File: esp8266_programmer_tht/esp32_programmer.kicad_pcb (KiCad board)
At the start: 2 copper layers, 67.2 x 66.5 mm, 41 parts, among them P1 USB_C_Plug_USB2.0, Q1 S8050, Q2 S8050, SW1 SW_Push, SW2 SW_Push, U1 CH340C, U2 ESP-12E

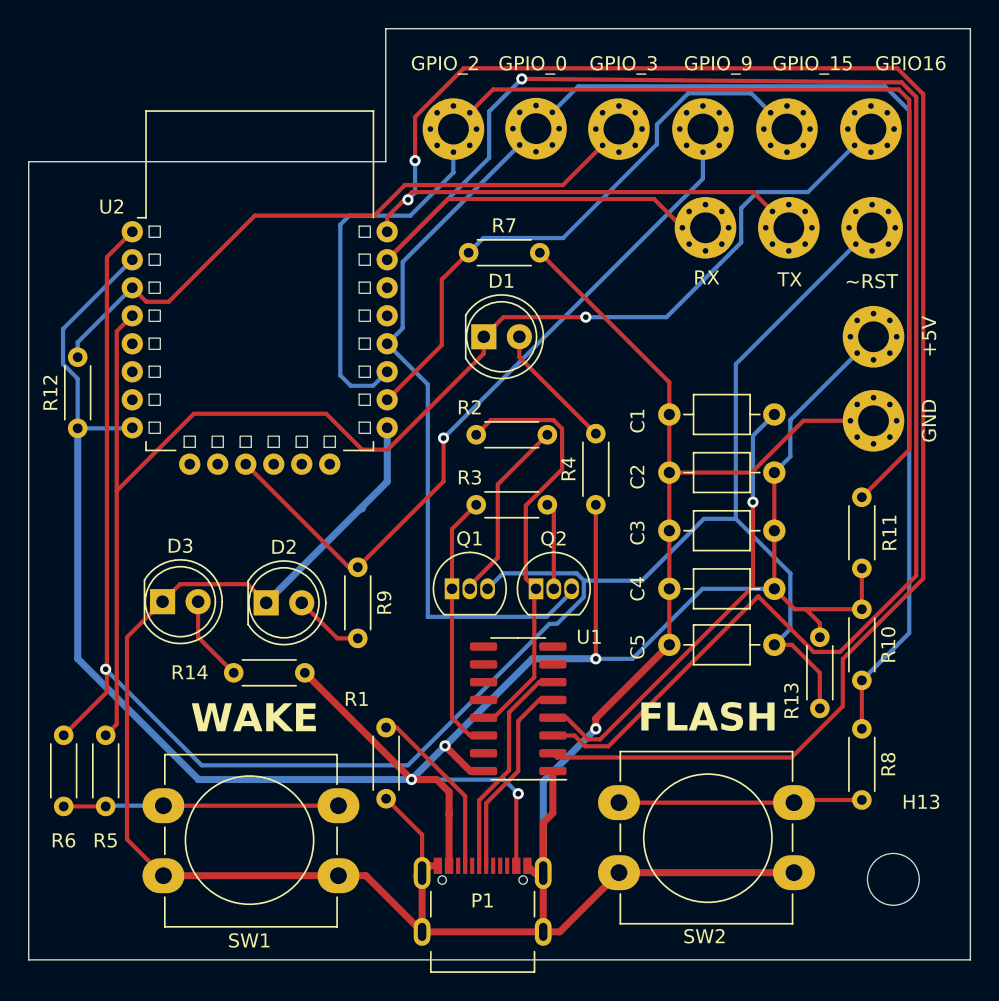
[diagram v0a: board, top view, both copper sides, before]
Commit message: esp8266 Programmer THT will GND Fill
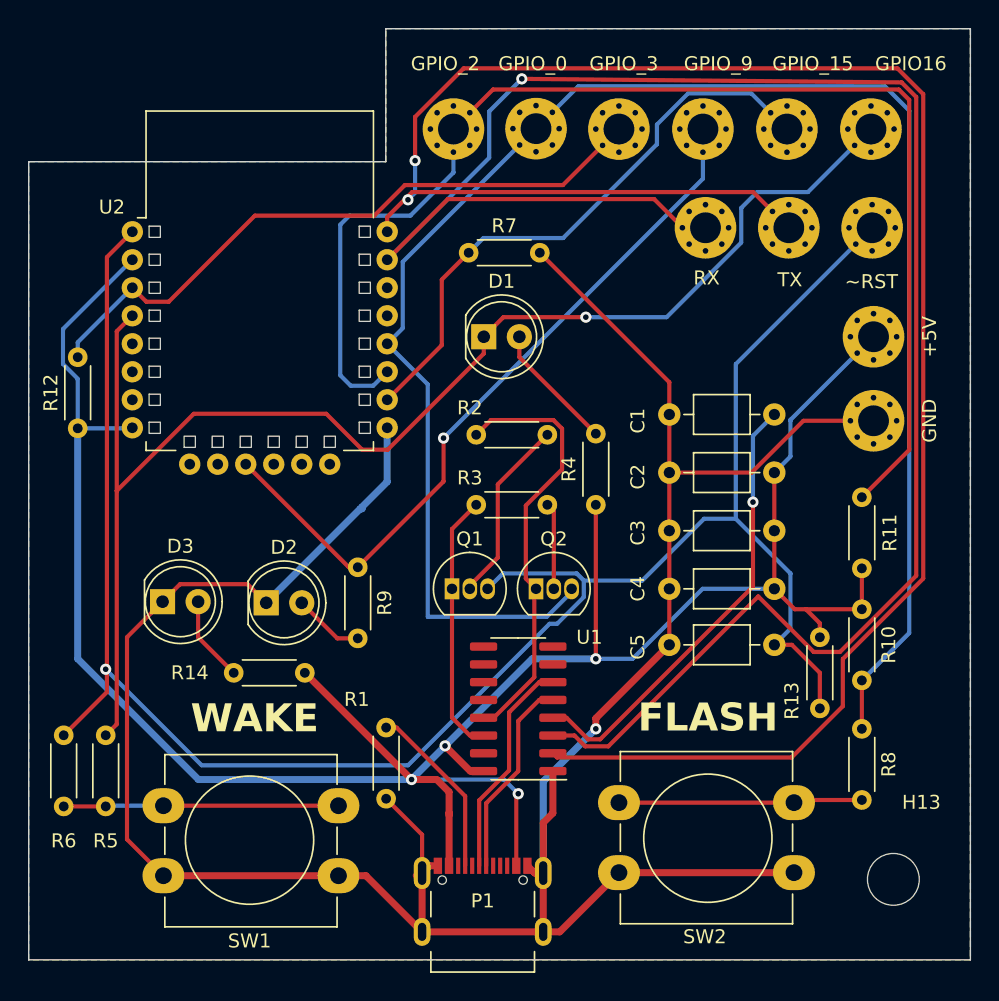
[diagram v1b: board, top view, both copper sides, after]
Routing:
- added copper zone on B.Cu, net GND
- added copper zone on F.Cu, net GND
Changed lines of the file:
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@@
   (segment (start 144.343015 136.08) (end 144.152143 136.270872) (width 0.3) (layer "F.Cu") (net 25))
   (segment (start 149 136.08) (end 144.343015 136.08) (width 0.3) (layer "F.Cu") (net 25))
+  (zone (net 1) (net_name "GND") (layers "F&B.Cu") (hatch edge 0.5)
+    (connect_pads (clearance 0.5))
+    (min_thickness 0.25) (filled_areas_thickness no)
+    (fill yes (thermal_gap 0.5) (thermal_bridge_width 0.5))
+    (polygon
+      (pts
+        (xy 115 81)
+        (xy 156.75 81)
+        (xy 156.75 147.5)
+        (xy 89.5 147.5)
+        (xy 89.5 90.5)
+        (xy 115 90.5)
+      )
+    )
+  )
 )

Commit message: D+ D- fixing
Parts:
- renumbered GPIO_9 to BOOT, GPIO_3 to EN, GPIO_0 to PIN0, GPIO_15 to PIN15, GPIO16 to PIN16, GPIO_2 to PIN2, ~RST to nRST
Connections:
- U1 pad 5: Net-(P1-D-) -> Net-(P1-D+)
- U1 pad 6: Net-(P1-D+) -> Net-(P1-D-)
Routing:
- net Net-(P1-D+): track 15.9 -> 0.97 mm
- net Net-(P1-D-): track 14.4 -> 0.97 mm
- net /PIN2: track 91.4 -> 94.0 mm
- net /RX: track 139.9 -> 141.3 mm
- net /TX: track 144.7 -> 146.1 mm
- net /BOOT_LED: track 52.6 -> 53.5 mm

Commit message: D+ D- pcb
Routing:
- net Net-(P1-D+): track 0.97 -> 17.1 mm, vias 0 -> 2
- net Net-(P1-D-): track 0.97 -> 16.7 mm
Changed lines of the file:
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@@
   (segment (start 111.75 105.75) (end 112.5 106.5) (width 0.3) (layer "B.Cu") (net 15))
   (segment (start 116.761269 94.35) (end 112.4 94.35) (width 0.3) (layer "B.Cu") (net 15))
-  (segment (start 115.773552 130.91147) (end 120.67 135.807918) (width 0.3) (layer "F.Cu") (net 16))
-  (segment (start 120.67 135.807918) (end 120.67 140.78) (width 0.3) (layer "F.Cu") (net 16))
   (segment (start 115.025581 130.91147) (end 115.773552 130.91147) (width 0.3) (layer "F.Cu") (net 16))
+  (segment (start 120.12 135.257918) (end 120.12 138.37) (width 0.3) (layer "F.Cu") (net 16))
+  (segment (start 115.773552 130.91147) (end 120.12 135.257918) (width 0.3) (layer "F.Cu") (net 16))
+  (segment (start 120.12 138.37) (end 120.67 138.92) (width 0.3) (layer "F.Cu") (net 16))
+  (segment (start 120.67 138.92) (end 120.67 140.78) (width 0.3) (layer "F.Cu") (net 16))
   (segment (start 126.935 128.936445) (end 125.960001 128.936445) (width 0.3) (layer "F.Cu") (net 17))
+  (segment (start 124.75 130.146446) (end 124.75 132.25) (width 0.3) (layer "F.Cu") (net 17))
+  (segment (start 121.108986 137.479965) (end 120.979965 137.479965) (width 0.25) (layer "F.Cu") (net 17))
+  (segment (start 121.67 140.78) (end 121.67 138.17) (width 0.25) (layer "F.Cu") (net 17))
+  (segment (start 121.108986 137.608986) (end 121.108986 137.479965) (width 0.25) (layer "F.Cu") (net 17))
+  (segment (start 121.67 138.17) (end 121.108986 137.608986) (width 0.25) (layer "F.Cu") (net 17))
+  (segment (start 120.979965 137.479965) (end 121 137.5) (width 0.25) (layer "F.Cu") (net 17))
+  (segment (start 125.960001 128.936445) (end 124.75 130.146446) (width 0.3) (layer "F.Cu") (net 17))
+  (via (at 121.108986 137.479965) (size 0.8) (drill 0.4) (layers "F.Cu" "B.Cu") (net 17))
+  (via (at 124.75 132.25) (size 0.8) (drill 0.4) (layers "F.Cu" "B.Cu") (net 17))
+  (segment (start 123.64134 137.479965) (end 125.25 135.871305) (width 0.25) (layer "B.Cu") (net 17))
+  (segment (start 125.25 132.75) (end 124.75 132.25) (width 0.25) (layer "B.Cu") (net 17))
+  (segment (start 121.108986 137.479965) (end 123.64134 137.479965) (width 0.25) (layer "B.Cu") (net 17))
+  (segment (start 125.25 135.871305) (end 125.25 132.75) (width 0.25) (layer "B.Cu") (net 17))
+  (segment (start 125.924646 127.666445) (end 126.935 127.666445) (width 0.25) (layer "F.Cu") (net 18))
+  (segment (start 122.17 135.482353) (end 123.545546 134.106807) (width 0.25) (layer "F.Cu") (net 18))
+  (segment (start 122.17 140.78) (end 122.17 135.482353) (width 0.25) (layer "F.Cu") (net 18))
   (segment (start 126.935 127.666445) (end 125.960001 127.666445) (width 0.3) (layer "F.Cu") (net 18))
+  (segment (start 123.545546 134.106807) (end 123.545546 130.045545) (width 0.25) (layer "F.Cu") (net 18))
+  (segment (start 123.545546 130.045545) (end 125.924646 127.666445) (width 0.25) (layer "F.Cu") (net 18))
   (segment (start 121.46 115) (end 119.73 116.73) (width 0.3) (layer "F.Cu") (net 20))
   (segment (start 119.73 130.196444) (end 121.010001 131.476445) (width 0.3) (layer "F.Cu") (net 20))
